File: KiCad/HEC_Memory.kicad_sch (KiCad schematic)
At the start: 10 parts, among them U12 74LS04, U13 74LS245, U14 74LS245, U15 74LS32, U16 74LS32, U2 AS6C4008-55PCN, U3 AS6C4008-55PCN, U4 CY7C199, U5 CY7C199, U9 74LS574

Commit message: Created footprint for HEC bus
Created footprints for HEC bus and some other updates.
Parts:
- U2, U3: footprint Package_DIP:DIP-32_W15.24mm -> Package_DIP:DIP-32_W15.24mm_Socket
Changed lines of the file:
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@@
       (effects (font (size 1.27 1.27)) (justify left))
     )
-    (property "Footprint" "Package_DIP:DIP-32_W15.24mm" (at 38.1 160.02 0)
+    (property "Footprint" "Package_DIP:DIP-32_W15.24mm_Socket" (at 38.1 160.02 0)
       (effects (font (size 1.27 1.27)) hide)
     )
@@
       (effects (font (size 1.27 1.27)) (justify left))
     )
-    (property "Footprint" "Package_DIP:DIP-32_W15.24mm" (at 86.36 160.02 0)
-      (effects (font (size 1.27 1.27)) hide)
-    )
+    (property "Footprint" "Package_DIP:DIP-32_W15.24mm_Socket" (at 86.36 160.02 0)
+      (effects (font (size 1.27 1.27)) hide)
+    )

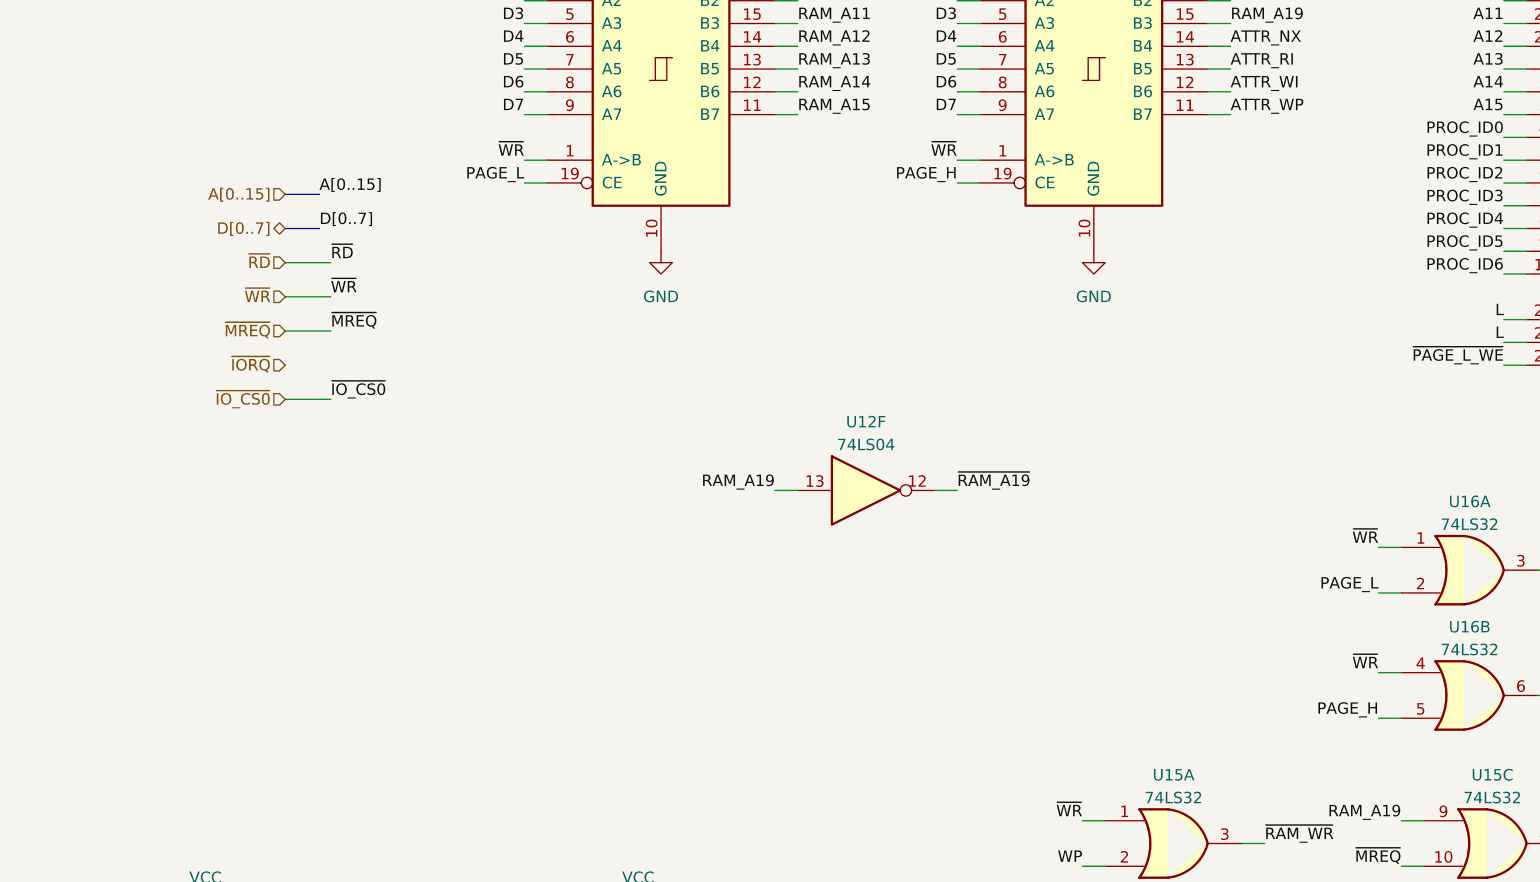
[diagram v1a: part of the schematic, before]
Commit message: IO implementation
Implemented most of IO functions, add connections between the schematics.
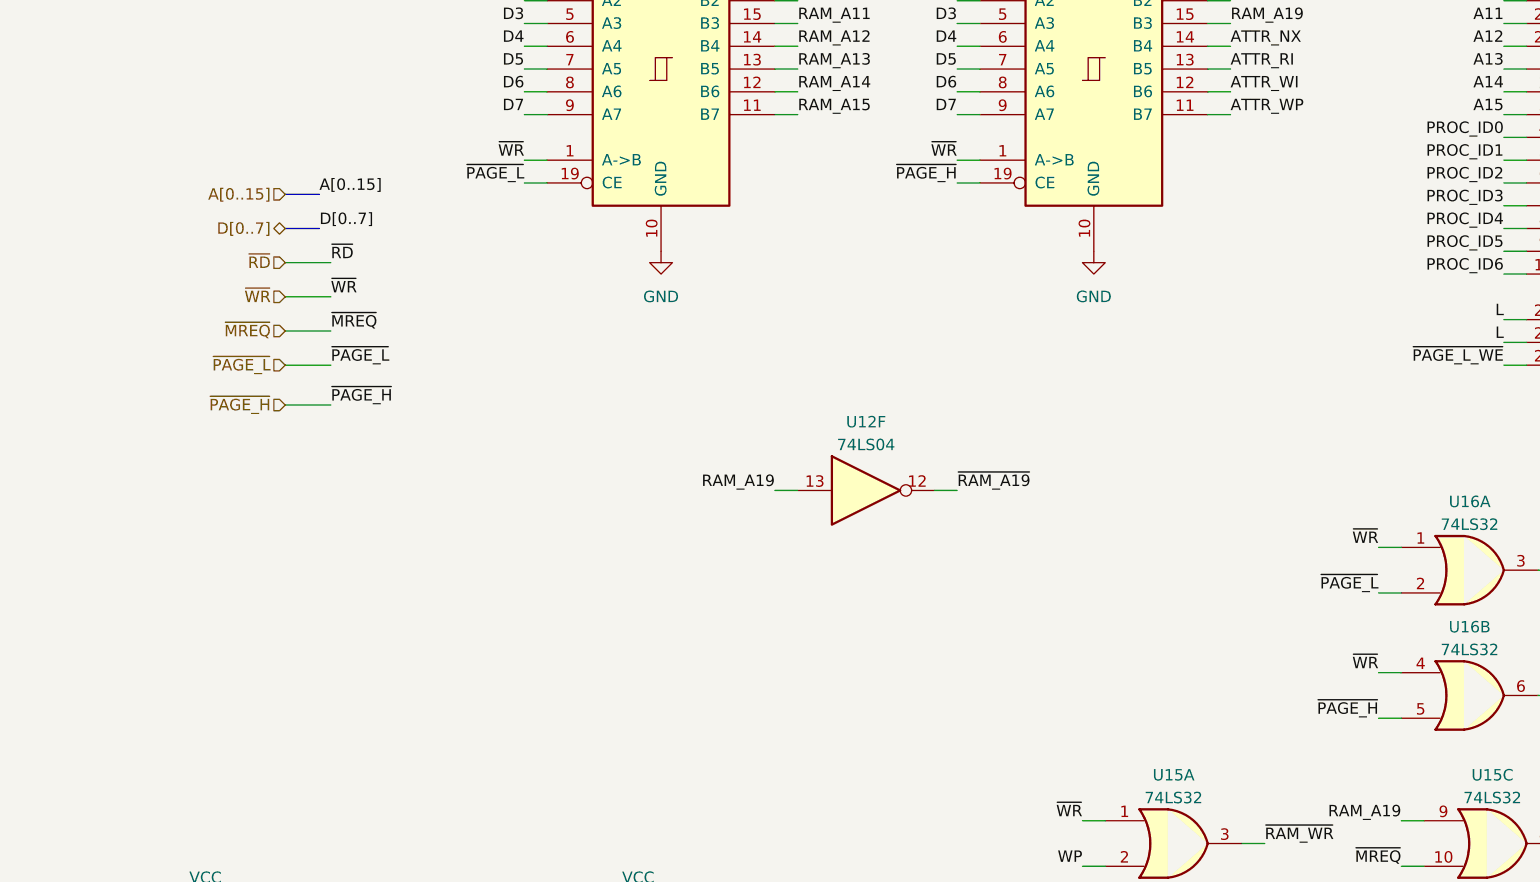
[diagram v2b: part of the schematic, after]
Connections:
- net PAGE_H renamed ~{PAGE_H}
- net PAGE_L renamed ~{PAGE_L}
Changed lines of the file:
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@@
+    (stroke (width 0) (type default))
+  )
+  (wire (pts (xy 46.99 78.105) (xy 52.07 78.105))
     (stroke (width 0) (type default))
   )
@@
     (stroke (width 0) (type default))
   )
+  (wire (pts (xy 46.99 73.66) (xy 52.07 73.66))
+    (stroke (width 0) (type default))
+  )
   (wire (pts (xy 124.46 30.48) (xy 121.92 30.48))
     (stroke (width 0) (type default))
@@
   )
   (wire (pts (xy 233.68 133.35) (xy 231.14 133.35))
-    (stroke (width 0) (type default))
-  )
-  (wire (pts (xy 46.99 77.47) (xy 52.07 77.47))
     (stroke (width 0) (type default))
   )
@@
     (effects (font (size 1.27 1.27)) (justify right bottom))
   )
+  (label "~{PAGE_L}" (at 52.07 73.66 0) (fields_autoplaced)
+    (effects (font (size 1.27 1.27)) (justify left bottom))
+  )
   (label "ATTR_RI" (at 152.4 40.64 0) (fields_autoplaced)
     (effects (font (size 1.27 1.27)) (justify left bottom))
@@
     (effects (font (size 1.27 1.27)) (justify right bottom))
   )
-  (label "PAGE_L" (at 73.66 53.34 180) (fields_autoplaced)
+  (label "~{PAGE_L}" (at 73.66 53.34 180) (fields_autoplaced)
     (effects (font (size 1.27 1.27)) (justify right bottom))
   )
@@
     (effects (font (size 1.27 1.27)) (justify right bottom))
   )
-  (label "PAGE_H" (at 121.92 53.34 180) (fields_autoplaced)
+  (label "~{PAGE_H}" (at 121.92 53.34 180) (fields_autoplaced)
     (effects (font (size 1.27 1.27)) (justify right bottom))
   )
@@
     (effects (font (size 1.27 1.27)) (justify left bottom))
   )
-  (label "~{IO_CS0}" (at 52.07 77.47 0) (fields_autoplaced)
-    (effects (font (size 1.27 1.27)) (justify left bottom))
-  )
   (label "A1" (at 71.12 142.24 180) (fields_autoplaced)
     (effects (font (size 1.27 1.27)) (justify right bottom))
@@
     (effects (font (size 1.27 1.27)) (justify right bottom))
   )
-  (label "PAGE_H" (at 168.91 113.03 180) (fields_autoplaced)
+  (label "~{PAGE_H}" (at 168.91 113.03 180) (fields_autoplaced)
     (effects (font (size 1.27 1.27)) (justify right bottom))
   )
@@
     (effects (font (size 1.27 1.27)) (justify left bottom))
   )
+  (label "~{PAGE_H}" (at 52.07 78.105 0) (fields_autoplaced)
+    (effects (font (size 1.27 1.27)) (justify left bottom))
+  )
   (label "RAM_A9" (at 71.12 162.56 180) (fields_autoplaced)
     (effects (font (size 1.27 1.27)) (justify right bottom))
@@
     (effects (font (size 1.27 1.27)) (justify right bottom))
   )
-  (label "PAGE_L" (at 168.91 99.06 180) (fields_autoplaced)
+  (label "~{PAGE_L}" (at 168.91 99.06 180) (fields_autoplaced)
     (effects (font (size 1.27 1.27)) (justify right bottom))
   )
@@
     (effects (font (size 1.27 1.27)) (justify right bottom))
   )
-  (hierarchical_label "~{IORQ}" (shape input) (at 46.99 73.66 180) (fields_autoplaced)
+  (hierarchical_label "~{PAGE_L}" (shape input) (at 46.99 73.66 180) (fields_autoplaced)
     (effects (font (size 1.27 1.27)) (justify right))
   )
@@
     (effects (font (size 1.27 1.27)) (justify right))
   )
-  (hierarchical_label "~{IO_CS0}" (shape input) (at 46.99 77.47 180) (fields_autoplaced)
+  (hierarchical_label "~{PAGE_H}" (shape input) (at 46.99 78.105 180) (fields_autoplaced)
     (effects (font (size 1.27 1.27)) (justify right))
   )

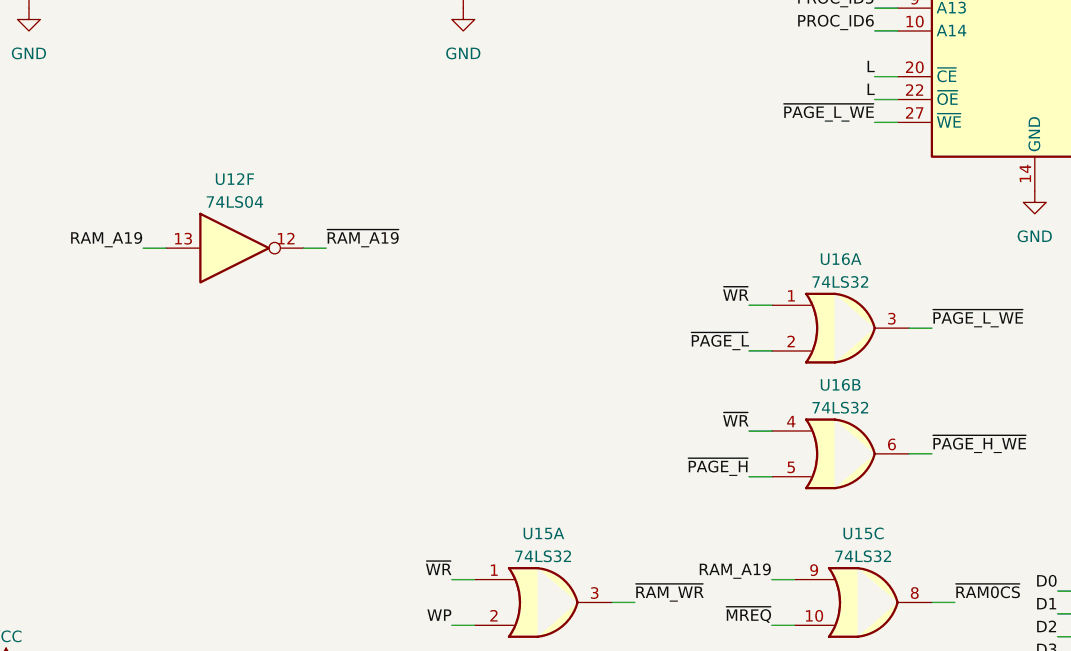
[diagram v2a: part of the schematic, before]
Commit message: Add wait state generator
Add circuit to generate 0 to 15 wait states or use external wait input.
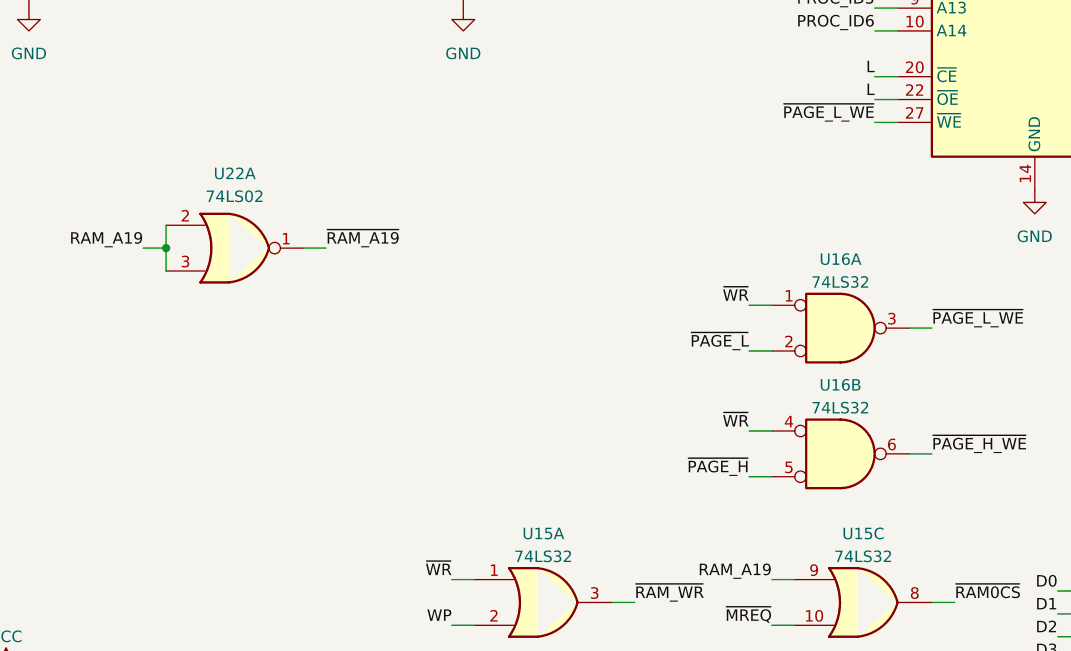
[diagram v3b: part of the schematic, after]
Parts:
- removed U12: 74LS04, Package_DIP:DIP-14_W7.62mm_Socket, symbol 74xx:74LS04
- added U22: 74LS02, Package_DIP:DIP-14_W7.62mm_Socket, symbol 74xx:74LS02
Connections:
- net RAM_A19: now also U22.2, U22.3
- net ~{RAM_A19}: now also U22.1

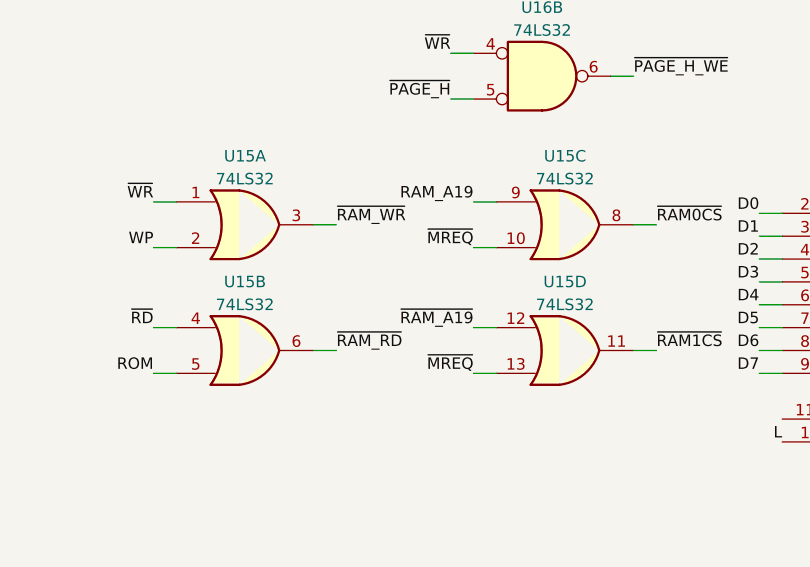
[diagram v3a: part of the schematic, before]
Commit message: Saved changes for added save state generator
Some changes for the wait state generator was not saved in the last commit
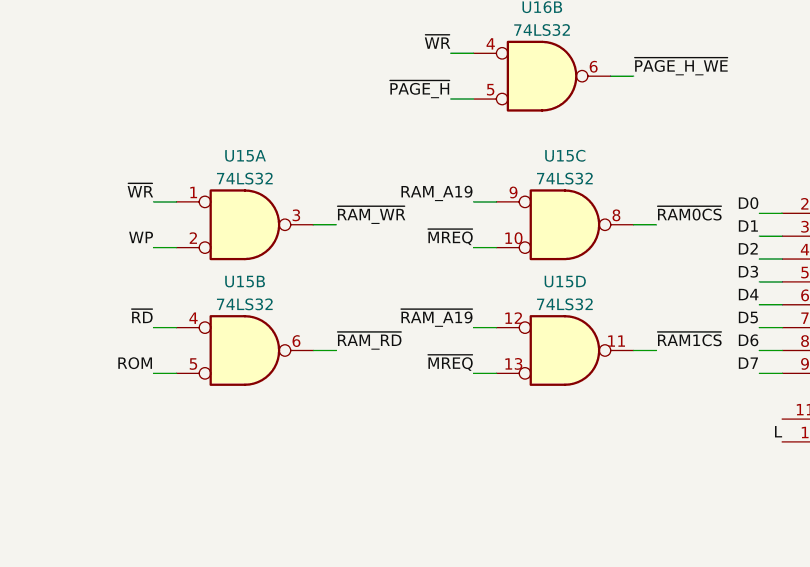
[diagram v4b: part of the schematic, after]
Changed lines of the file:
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@@
     )
   )
-  (symbol (lib_id "74xx:74LS32") (at 181.61 127 0) (unit 3)
+  (symbol (lib_id "74xx:74LS32") (at 181.61 127 0) (unit 3) (convert 2)
     (in_bom yes) (on_board yes) (dnp no) (fields_autoplaced)
     (property "Reference" "U15" (at 181.61 119.38 0)
@@
     )
   )
-  (symbol (lib_id "74xx:74LS32") (at 146.05 140.97 0) (unit 2)
+  (symbol (lib_id "74xx:74LS32") (at 146.05 140.97 0) (unit 2) (convert 2)
     (in_bom yes) (on_board yes) (dnp no) (fields_autoplaced)
     (property "Reference" "U15" (at 146.05 133.35 0)
@@
     )
   )
-  (symbol (lib_id "74xx:74LS32") (at 181.61 140.97 0) (unit 4)
+  (symbol (lib_id "74xx:74LS32") (at 181.61 140.97 0) (unit 4) (convert 2)
     (in_bom yes) (on_board yes) (dnp no) (fields_autoplaced)
     (property "Reference" "U15" (at 181.61 133.35 0)
@@
     )
   )
-  (symbol (lib_id "74xx:74LS32") (at 146.05 127 0) (unit 1)
+  (symbol (lib_id "74xx:74LS32") (at 146.05 127 0) (unit 1) (convert 2)
     (in_bom yes) (on_board yes) (dnp no) (fields_autoplaced)
     (property "Reference" "U15" (at 146.05 119.38 0)
